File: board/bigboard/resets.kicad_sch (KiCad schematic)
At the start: 13 parts, among them J12 Conn_01x03_Male, J13 Conn_02x07_Row_Letter_First, SW6 SW_Push, SW7 SW_Push, SW8 SW_Push, U11 TXB0104D

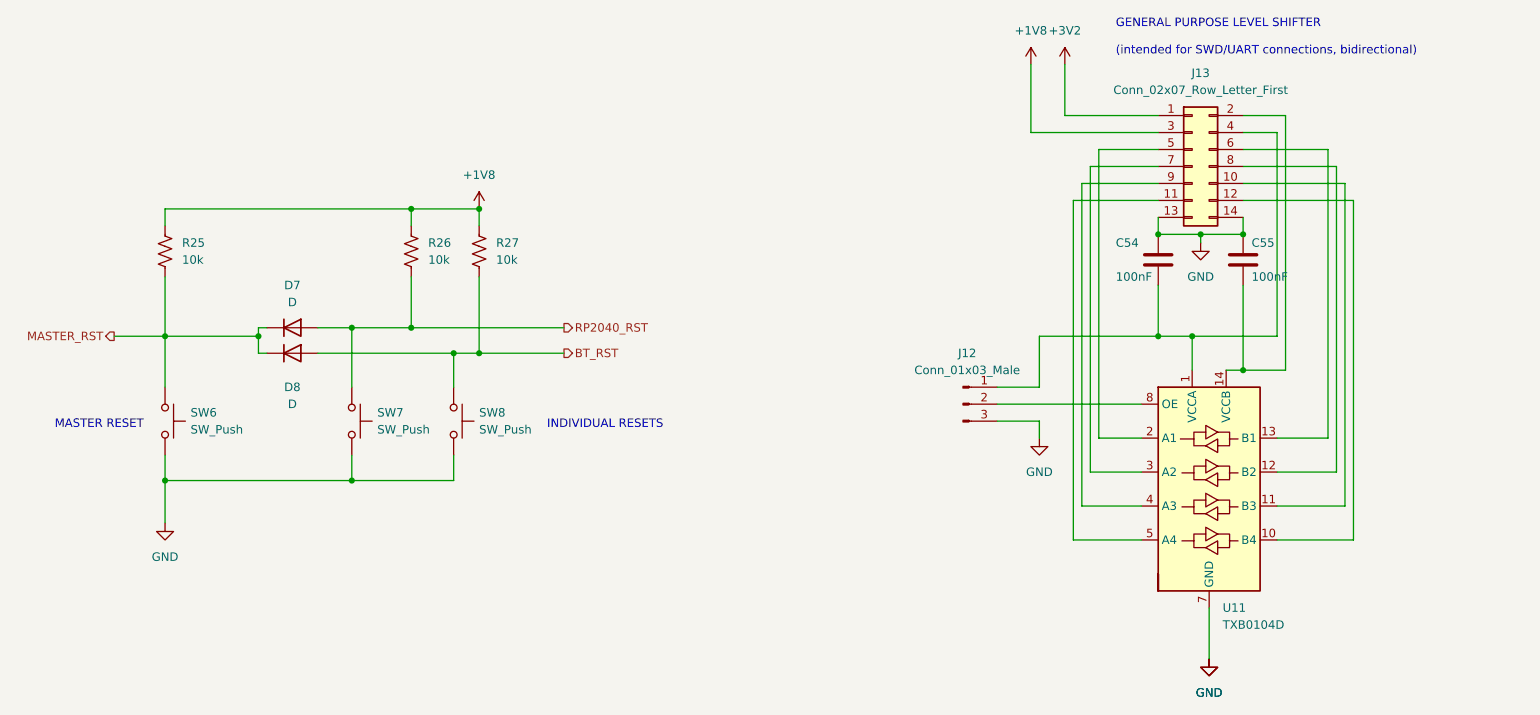
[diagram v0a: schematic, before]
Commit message: Manufactured version of bigboard
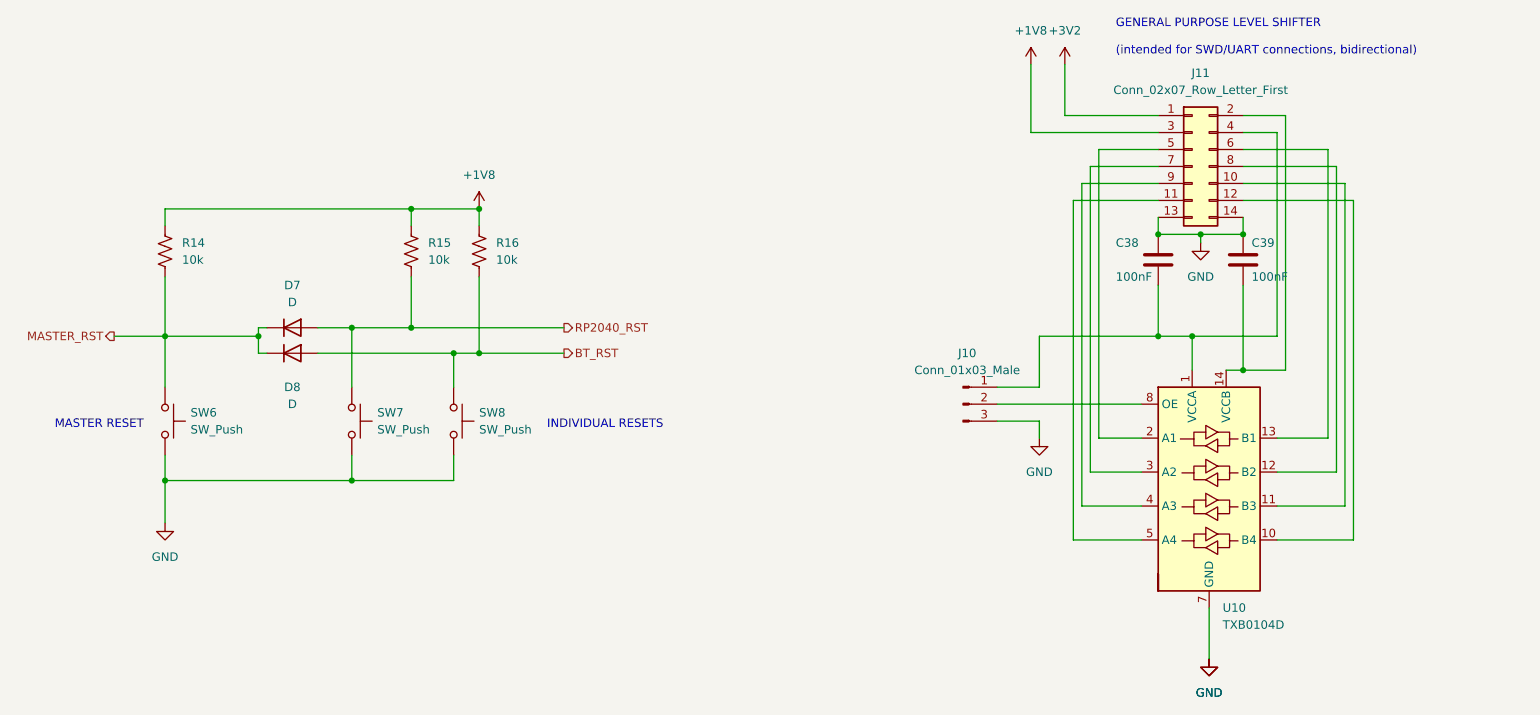
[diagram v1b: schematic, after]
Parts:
- C38: renamed from C54; MPN (none) -> CC0201KRX5R8BB104
- C39: renamed from C55; MPN (none) -> CC0201KRX5R8BB104
- R14: renamed from R25; MPN (none) -> RC0201FR-0710KL
- R15: renamed from R26; MPN (none) -> RC0201FR-0710KL
- R16: renamed from R27; MPN (none) -> RC0201FR-0710KL
- renumbered J12 to J10, J13 to J11, U11 to U10
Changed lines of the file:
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@@
   (symbol (lib_id "Logic_LevelTranslator:TXB0104D") (at 219.71 118.11 0) (unit 1)
     (in_bom yes) (on_board yes) (fields_autoplaced)
-    (property "Reference" "U11" (id 0) (at 221.7294 135.89 0)
+    (property "Reference" "U10" (id 0) (at 221.7294 135.89 0)
       (effects (font (size 1.27 1.27)) (justify left))
     )
@@
   (symbol (lib_id "power:+1V8") (at 193.04 54.61 0) (unit 1)
     (in_bom yes) (on_board yes) (fields_autoplaced)
-    (property "Reference" "#PWR045" (id 0) (at 193.04 58.42 0)
+    (property "Reference" "#PWR041" (id 0) (at 193.04 58.42 0)
       (effects (font (size 1.27 1.27)) hide)
     )
@@
   (symbol (lib_id "3v2:+3V2") (at 198.12 54.61 0) (unit 1)
     (in_bom yes) (on_board yes) (fields_autoplaced)
-    (property "Reference" "#PWR047" (id 0) (at 198.12 58.42 0)
+    (property "Reference" "#PWR043" (id 0) (at 198.12 58.42 0)
       (effects (font (size 1.27 1.27)) hide)
     )
@@
   (symbol (lib_id "Connector:Conn_01x03_Male") (at 182.88 105.41 0) (unit 1)
     (in_bom yes) (on_board yes) (fields_autoplaced)
-    (property "Reference" "J12" (id 0) (at 183.515 97.79 0))
+    (property "Reference" "J10" (id 0) (at 183.515 97.79 0))
     (property "Value" "Conn_01x03_Male" (id 1) (at 183.515 100.33 0))
     (property "Footprint" "Connector_PinHeader_2.54mm:PinHeader_1x03_P2.54mm_Vertical" (id 2) (at 182.88 105.41 0)
@@
   (symbol (lib_id "Device:C") (at 224.79 83.82 0) (unit 1)
     (in_bom yes) (on_board yes)
-    (property "Reference" "C55" (id 0) (at 226.06 81.28 0)
+    (property "Reference" "C39" (id 0) (at 226.06 81.28 0)
       (effects (font (size 1.27 1.27)) (justify left))
     )
@@
       (effects (font (size 1.27 1.27)) hide)
     )
+    (property "MPN" "CC0201KRX5R8BB104" (id 5) (at 224.79 83.82 0)
+      (effects (font (size 1.27 1.27)) hide)
+    )
     (pin "1")
     (pin "2")
@@
   (symbol (lib_id "power:GND") (at 194.31 110.49 0) (unit 1)
     (in_bom yes) (on_board yes) (fields_autoplaced)
-    (property "Reference" "#PWR046" (id 0) (at 194.31 116.84 0)
+    (property "Reference" "#PWR042" (id 0) (at 194.31 116.84 0)
       (effects (font (size 1.27 1.27)) hide)
     )
@@
   (symbol (lib_id "power:GND") (at 63.5 123.19 0) (unit 1)
     (in_bom yes) (on_board yes) (fields_autoplaced)
-    (property "Reference" "#PWR043" (id 0) (at 63.5 129.54 0)
+    (property "Reference" "#PWR039" (id 0) (at 63.5 129.54 0)
       (effects (font (size 1.27 1.27)) hide)
     )
@@
   (symbol (lib_id "Device:R_US") (at 63.5 82.55 0) (unit 1)
     (in_bom yes) (on_board yes) (fields_autoplaced)
-    (property "Reference" "R25" (id 0) (at 66.04 81.2799 0)
+    (property "Reference" "R14" (id 0) (at 66.04 81.2799 0)
       (effects (font (size 1.27 1.27)) (justify left))
     )
@@
       (effects (font (size 1.27 1.27)) hide)
     )
+    (property "MPN" "RC0201FR-0710KL" (id 5) (at 63.5 82.55 0)
+      (effects (font (size 1.27 1.27)) hide)
+    )
     (pin "1")
     (pin "2")
@@
   (symbol (lib_id "power:GND") (at 219.71 143.51 0) (unit 1)
     (in_bom yes) (on_board yes) (fields_autoplaced)
-    (property "Reference" "#PWR049" (id 0) (at 219.71 149.86 0)
+    (property "Reference" "#PWR045" (id 0) (at 219.71 149.86 0)
       (effects (font (size 1.27 1.27)) hide)
     )
@@
   (symbol (lib_id "power:+1V8") (at 110.49 76.2 0) (unit 1)
     (in_bom yes) (on_board yes) (fields_autoplaced)
-    (property "Reference" "#PWR044" (id 0) (at 110.49 80.01 0)
+    (property "Reference" "#PWR040" (id 0) (at 110.49 80.01 0)
       (effects (font (size 1.27 1.27)) hide)
     )
@@
   (symbol (lib_id "power:GND") (at 219.71 143.51 0) (unit 1)
     (in_bom yes) (on_board yes) (fields_autoplaced)
-    (property "Reference" "#PWR050" (id 0) (at 219.71 149.86 0)
+    (property "Reference" "#PWR046" (id 0) (at 219.71 149.86 0)
       (effects (font (size 1.27 1.27)) hide)
     )
@@
   (symbol (lib_id "Device:C") (at 212.09 83.82 0) (unit 1)
     (in_bom yes) (on_board yes)
-    (property "Reference" "C54" (id 0) (at 205.74 81.28 0)
+    (property "Reference" "C38" (id 0) (at 205.74 81.28 0)
       (effects (font (size 1.27 1.27)) (justify left))
     )
@@
       (effects (font (size 1.27 1.27)) hide)
     )
+    (property "MPN" "CC0201KRX5R8BB104" (id 5) (at 212.09 83.82 0)
+      (effects (font (size 1.27 1.27)) hide)
+    )
     (pin "1")
     (pin "2")
@@
   (symbol (lib_id "Connector_Generic:Conn_02x07_Odd_Even") (at 217.17 69.85 0) (unit 1)
     (in_bom yes) (on_board yes) (fields_autoplaced)
-    (property "Reference" "J13" (id 0) (at 218.44 55.88 0))
+    (property "Reference" "J11" (id 0) (at 218.44 55.88 0))
     (property "Value" "Conn_02x07_Row_Letter_First" (id 1) (at 218.44 58.42 0))
     (property "Footprint" "Connector_PinHeader_2.54mm:PinHeader_2x07_P2.54mm_Vertical" (id 2) (at 217.17 69.85 0)
@@
   (symbol (lib_id "Device:R_US") (at 100.33 82.55 0) (unit 1)
     (in_bom yes) (on_board yes) (fields_autoplaced)
-    (property "Reference" "R26" (id 0) (at 102.87 81.2799 0)
+    (property "Reference" "R15" (id 0) (at 102.87 81.2799 0)
       (effects (font (size 1.27 1.27)) (justify left))
     )
@@
     )
     (property "Description" "RES SMD 10KOHM 1% 1/20W 0201" (id 4) (at 100.33 82.55 0)
+      (effects (font (size 1.27 1.27)) hide)
+    )
+    (property "MPN" "RC0201FR-0710KL" (id 5) (at 100.33 82.55 0)
       (effects (font (size 1.27 1.27)) hide)
     )
@@
   (symbol (lib_id "Device:R_US") (at 110.49 82.55 0) (unit 1)
     (in_bom yes) (on_board yes) (fields_autoplaced)
-    (property "Reference" "R27" (id 0) (at 113.03 81.2799 0)
+    (property "Reference" "R16" (id 0) (at 113.03 81.2799 0)
       (effects (font (size 1.27 1.27)) (justify left))
     )
@@
     )
     (property "Description" "RES SMD 10KOHM 1% 1/20W 0201" (id 4) (at 110.49 82.55 0)
+      (effects (font (size 1.27 1.27)) hide)
+    )
+    (property "MPN" "RC0201FR-0710KL" (id 5) (at 110.49 82.55 0)
       (effects (font (size 1.27 1.27)) hide)
     )
@@
   (symbol (lib_id "power:GND") (at 218.44 81.28 0) (unit 1)
     (in_bom yes) (on_board yes) (fields_autoplaced)
-    (property "Reference" "#PWR048" (id 0) (at 218.44 87.63 0)
-      (effects (font (size 1.27 1.27)) hide)
-    )
+    (property "Reference" "#PWR044" (id 0) (at 218.44 87.63 0)
+      (effects (font (size 1.27 1.27)) hide)
+    )
